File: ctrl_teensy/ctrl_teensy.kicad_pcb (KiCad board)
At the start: 2 copper layers, 7 parts, among them P1 CONN_01X02, P2 CONN_01X13, P3 CONN_01X13, P4 CONN_01X02, U1 teensy

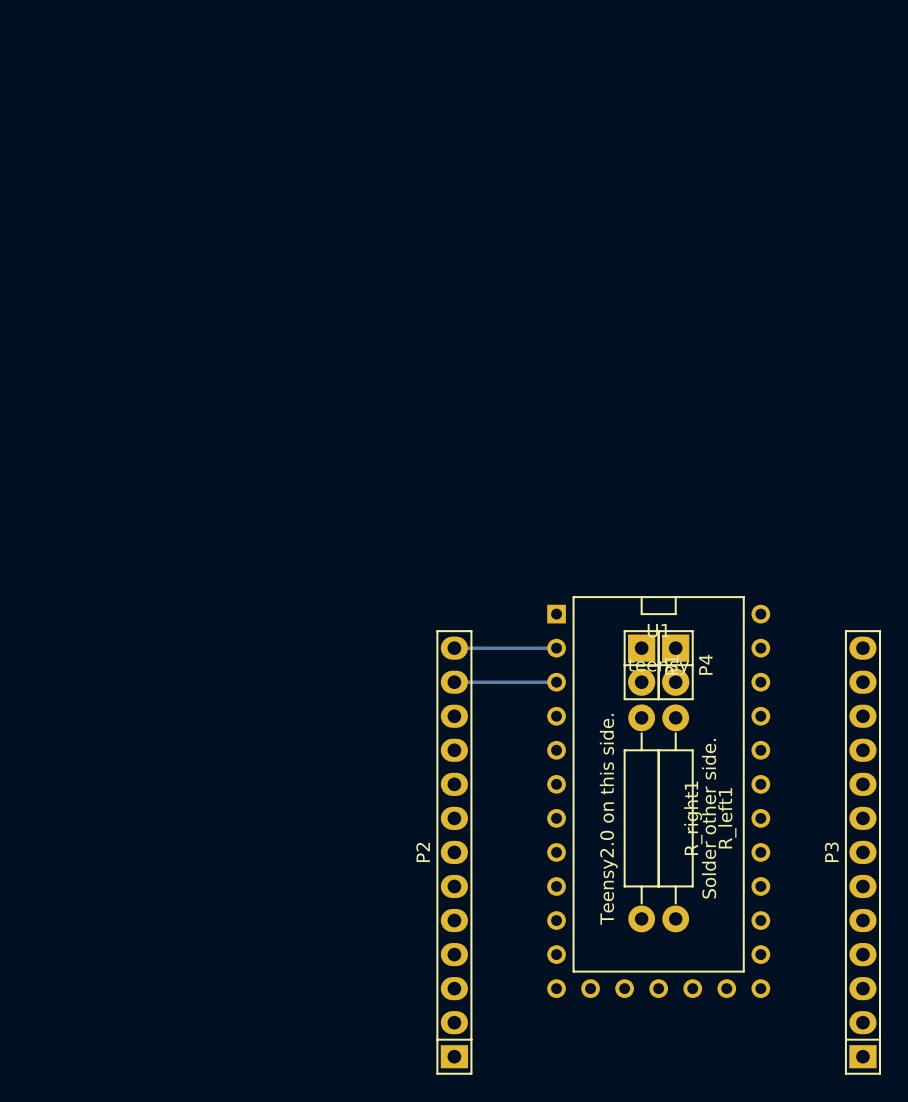
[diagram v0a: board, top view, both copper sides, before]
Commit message: Updated Lolly's first board which is now sent off to Seeed Studio for production.
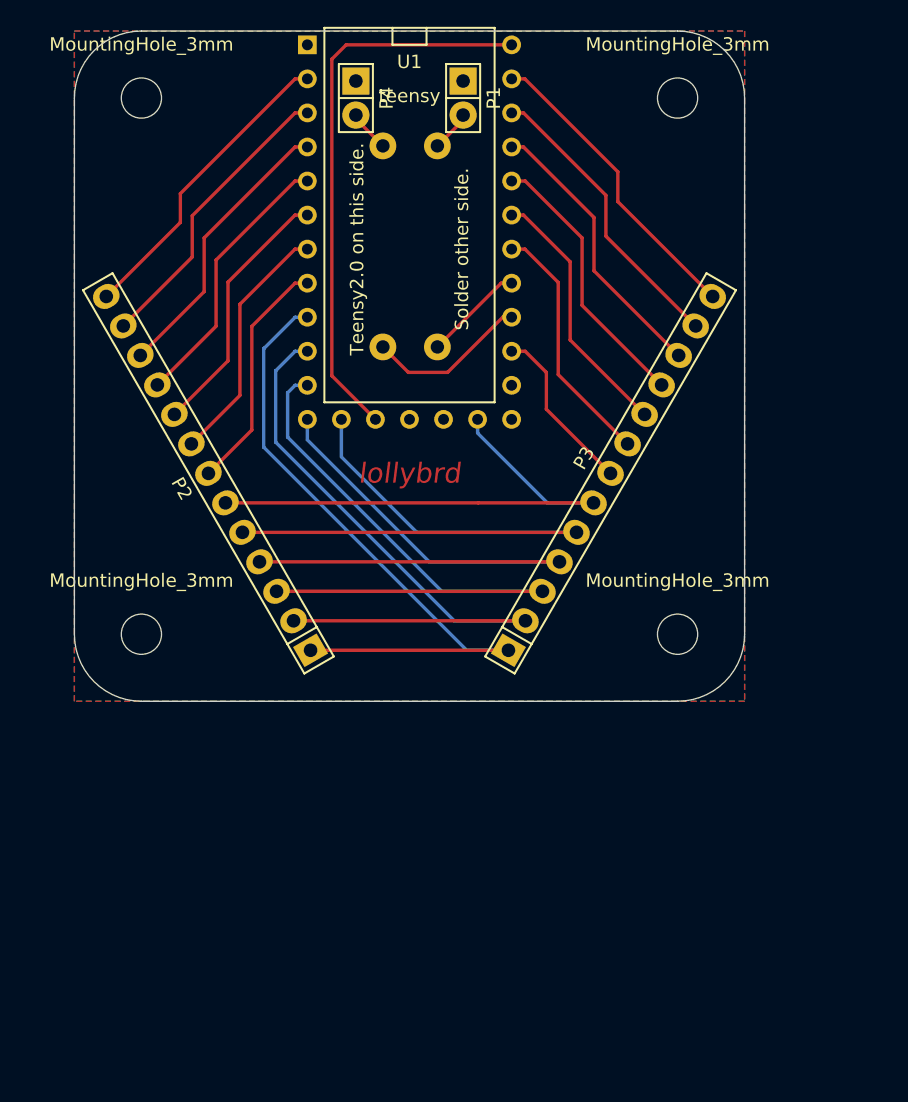
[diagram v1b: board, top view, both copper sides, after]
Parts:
- removed R_left1, R_right1: 220R, Resistors_ThroughHole:Resistor_Horizontal_RM15mm
- added MountingHole_3mm: VAL**, Mounting_Holes:MountingHole_3mm, F.Cu at (110.0, 65.0)
- added MountingHole_3mm: VAL**, Mounting_Holes:MountingHole_3mm, F.Cu at (150.0, 65.0)
- added MountingHole_3mm: VAL**, Mounting_Holes:MountingHole_3mm, F.Cu at (150.0, 25.0)
- added MountingHole_3mm: VAL**, Mounting_Holes:MountingHole_3mm, F.Cu at (110.0, 25.0)
- added R0: 220R, Resistors_ThroughHole:Resistor_Horizontal_RM15mm, B.Cu at (132.1, 36.1)
- added R1: 220R, Resistors_ThroughHole:Resistor_Horizontal_RM15mm, B.Cu at (128.0, 36.1)
- moved P4 48.6 mm to (126.0, 25.0)
- moved U1 46.4 mm to (130.0, 35.0)
- moved P1 44.4 mm to (134.0, 25.0)
- moved P3 34.0 mm to (145.0, 53.0), turned to 60 degrees
- moved P2 33.7 mm to (115.0, 53.0), turned to 120 degrees
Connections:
- P1 pad 2: ledR -> led0
- P4 pad 2: ledL -> led1
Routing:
- net col5: track 0.00 -> 50.9 mm
- net col4: track 0.00 -> 49.8 mm
- net col3: track 0.00 -> 48.6 mm
- net col1: track 0.00 -> 47.6 mm
- net col2: track 0.00 -> 46.5 mm
- net Net-(U1-PadVCC): track 0.00 -> 42.1 mm
- net col0: track 0.00 -> 39.3 mm
- net row6: track 0.00 -> 23.0 mm
- net row5: track 0.00 -> 22.1 mm
- net row9: track 0.00 -> 21.2 mm
- net row4: track 0.00 -> 21.2 mm
- net row3: track 0.00 -> 20.4 mm
- net rowA: track 0.00 -> 20.4 mm
- net rowB: track 0.00 -> 19.5 mm
- net row2: track 0.00 -> 19.5 mm
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- added copper zone on B.Cu, net GND
- added copper zone on F.Cu, net GND
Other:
- board outline added: 50 x 50 mm
- board text added: "lollybrd"
